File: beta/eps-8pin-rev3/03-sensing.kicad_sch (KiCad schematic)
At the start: 16 parts, among them U10 INA238, U11 INA238, U20 INA181A2IDBVR, U21 INA181A2IDBVR, U30 TLV7011DBVR, U31 TLV7011DBVR

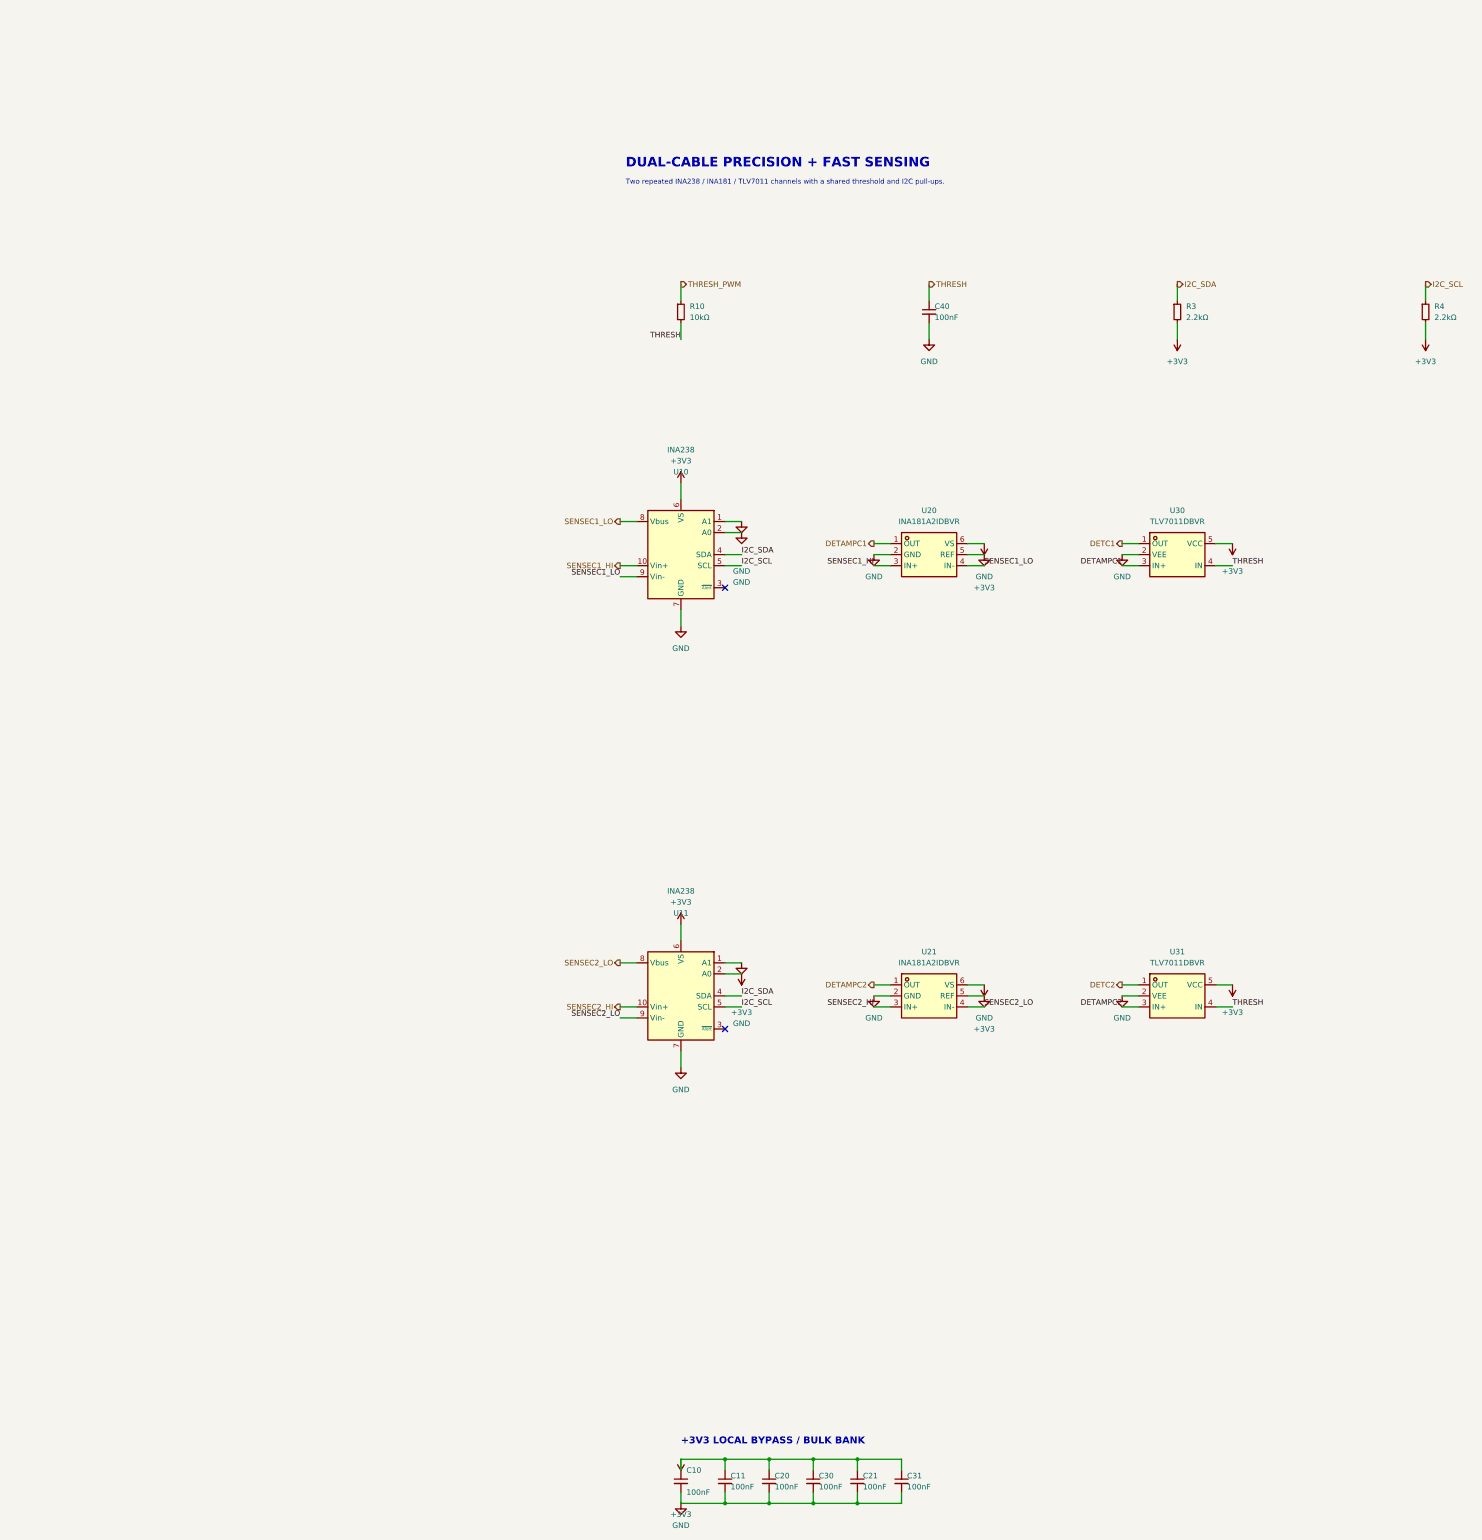
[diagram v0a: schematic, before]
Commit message: Enforce readable BETA schematic layouts
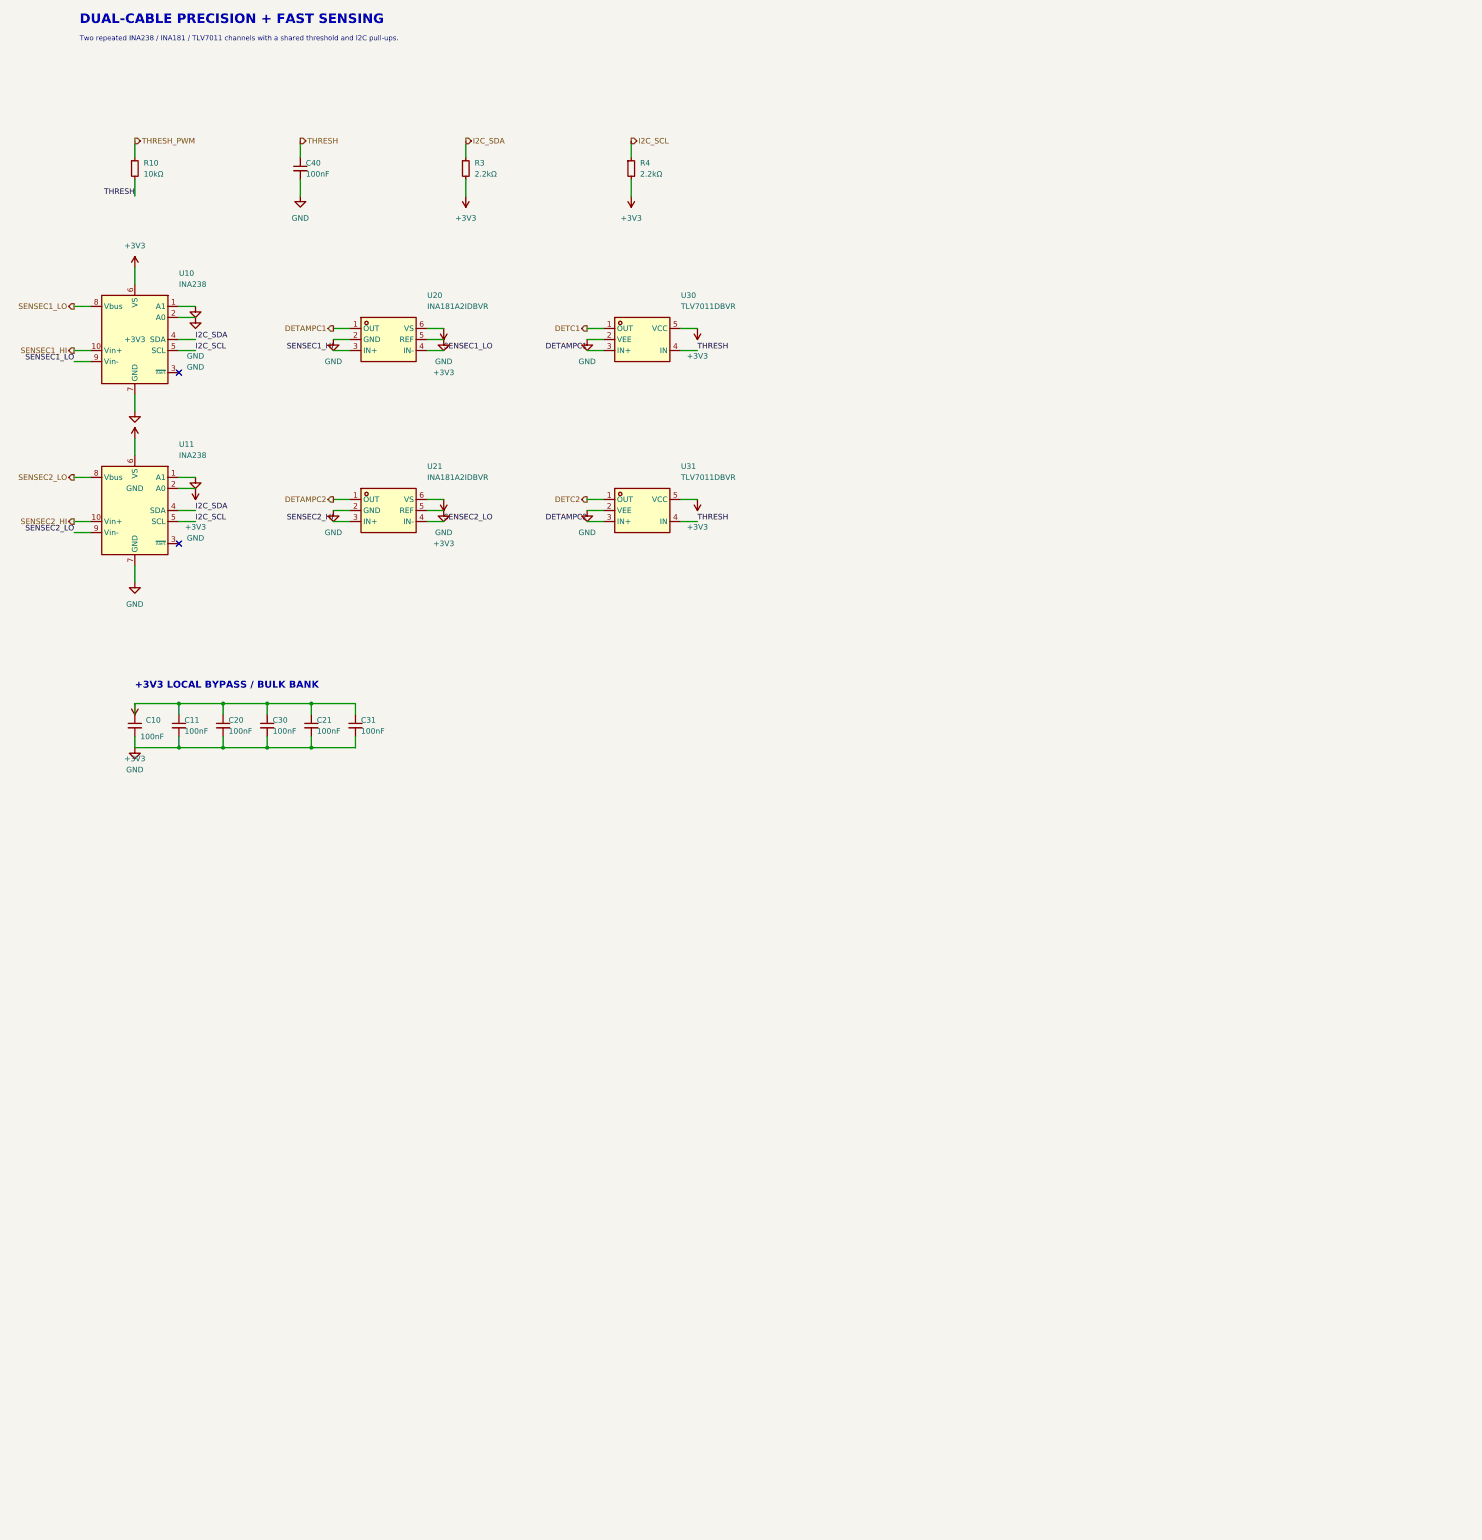
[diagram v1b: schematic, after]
